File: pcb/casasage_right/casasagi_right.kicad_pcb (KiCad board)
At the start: 2 copper layers, 133.3 x 82.7 mm, 114 parts, among them J1 USB_C_Receptacle_USB2.0, J2 AudioJack4, J3 Conn_01x05, SW1 RESET, SW2 BOOT, U1 TLV73333PDBV, U2 STM32F072C8Tx, U3 AT24CS32-XHM, Y1 8MHz

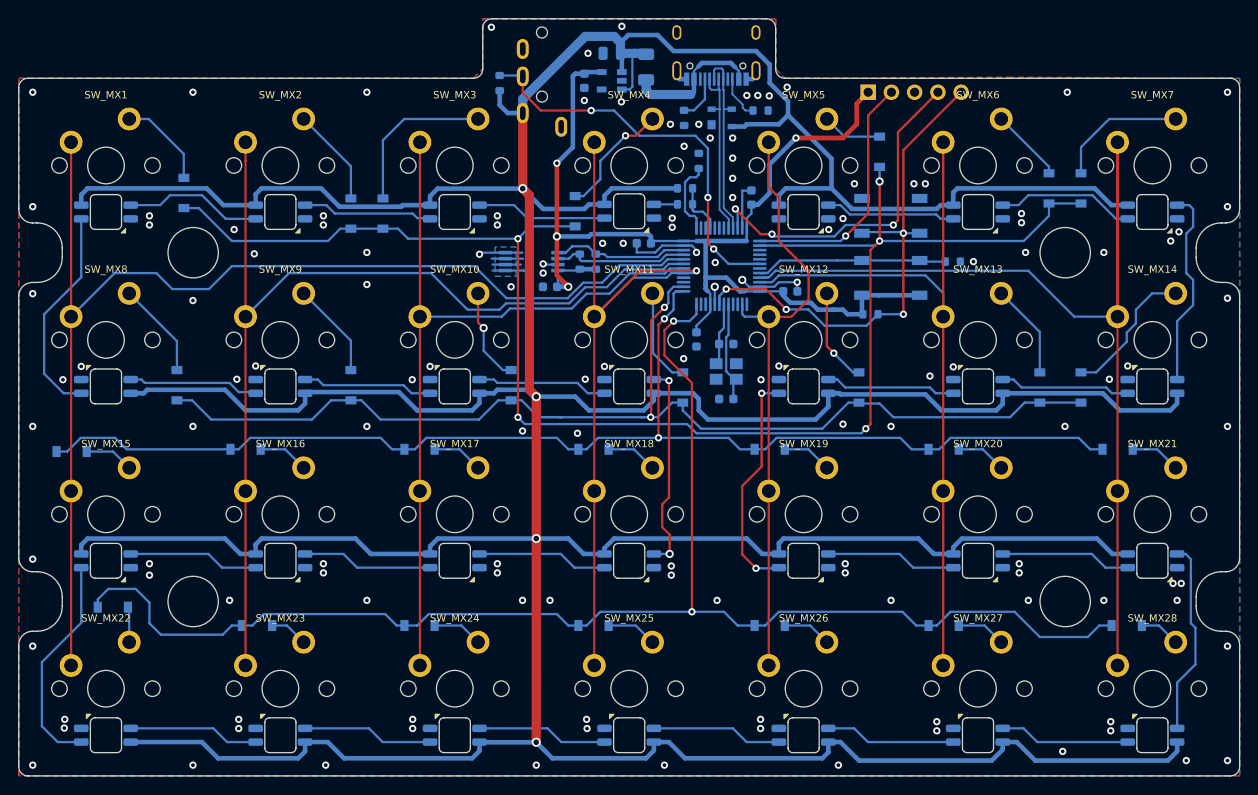
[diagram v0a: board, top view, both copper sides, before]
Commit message: update reference number for panelization
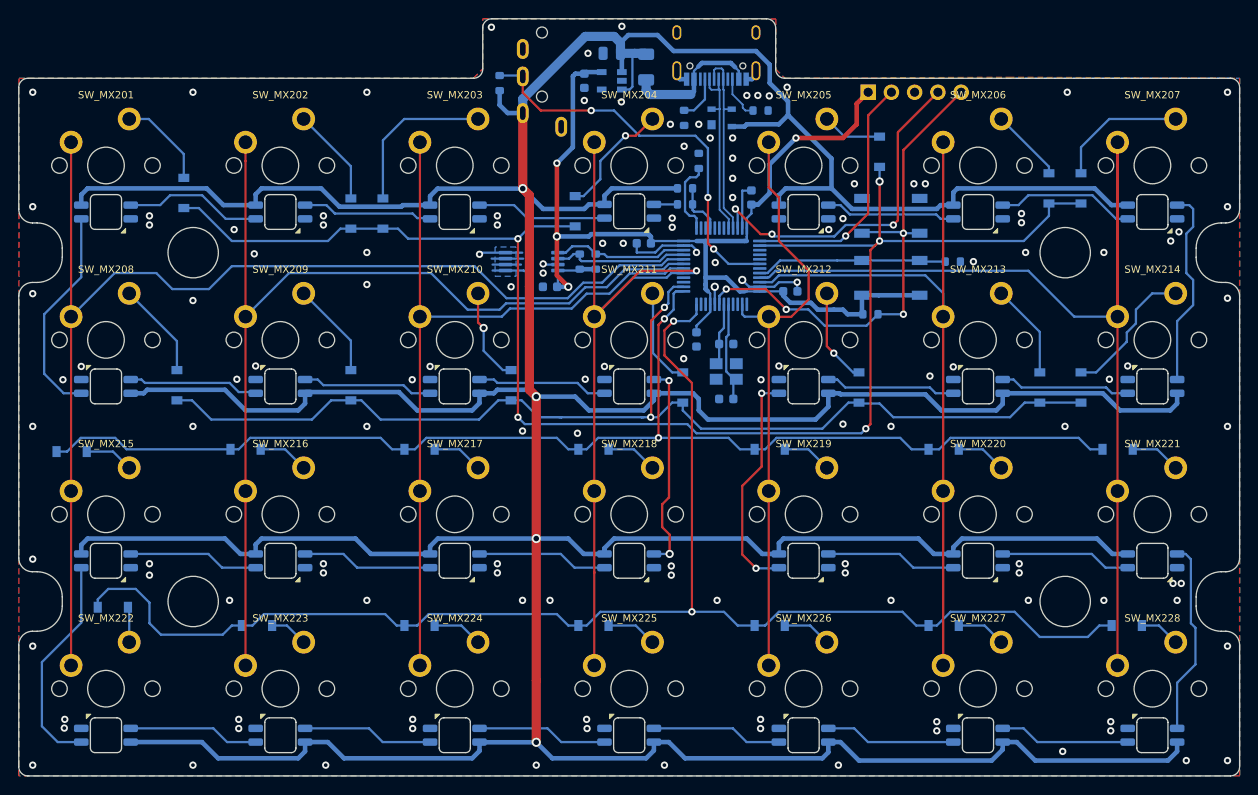
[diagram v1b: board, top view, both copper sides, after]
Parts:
- renumbered C1 to C201, C2 to C202, C9 to C203, C7 to C204, C3 to C205, C4 to C206, C5 to C207, C6 to C208, C8 to C209, D1 to D201, D2 to D202, D3 to D203, D4 to D204, D5 to D205, D6 to D206, D7 to D207, D8 to D208, D9 to D209, D10 to D210, D11 to D211, D12 to D212, D13 to D213, D14 to D214, D15 to D215, D16 to D216, D17 to D217, D18 to D218, D19 to D219, D20 to D220, D21 to D221, D22 to D222, D23 to D223, D24 to D224, D25 to D225, D26 to D226, D27 to D227, D28 to D228, D29 to D229, F1 to F201, J1 to J201, J2 to J202, J3 to J203, LED1 to LED201, LED2 to LED202, LED3 to LED203, LED4 to LED204, LED5 to LED205, LED6 to LED206, LED7 to LED207, LED8 to LED208, LED9 to LED209, LED10 to LED210, LED11 to LED211, LED12 to LED212, LED13 to LED213, LED14 to LED214, LED15 to LED215, LED16 to LED216, LED17 to LED217, LED18 to LED218, LED19 to LED219, LED20 to LED220, LED21 to LED221, LED22 to LED222, LED23 to LED223, LED24 to LED224, LED25 to LED225, LED26 to LED226, LED27 to LED227, LED28 to LED228, R1 to R201, R2 to R202, R6 to R203, R7 to R204, R3 to R205, R4 to R206, R9 to R207, R5 to R208, R10 to R209, R8 to R210, SW1 to SW201, SW2 to SW202, SW_MX1 to SW_MX201, SW_MX2 to SW_MX202, SW_MX3 to SW_MX203, SW_MX4 to SW_MX204, SW_MX5 to SW_MX205, SW_MX6 to SW_MX206, SW_MX7 to SW_MX207, SW_MX8 to SW_MX208, SW_MX9 to SW_MX209, SW_MX10 to SW_MX210, SW_MX11 to SW_MX211, SW_MX12 to SW_MX212, SW_MX13 to SW_MX213, SW_MX14 to SW_MX214, SW_MX15 to SW_MX215, SW_MX16 to SW_MX216, SW_MX17 to SW_MX217, SW_MX18 to SW_MX218, SW_MX19 to SW_MX219, SW_MX20 to SW_MX220, SW_MX21 to SW_MX221, SW_MX22 to SW_MX222, SW_MX23 to SW_MX223, SW_MX24 to SW_MX224, SW_MX25 to SW_MX225, SW_MX26 to SW_MX226, SW_MX27 to SW_MX227, SW_MX28 to SW_MX228, U1 to U201, U3 to U202, U2 to U203, Y1 to Y201

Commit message: add copyright on pcbs
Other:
- board text added: "(c) 2020, SMKiJ Casasagi Contributors"
- board text added: "Casasagi Right PCB / Rev. Alpha"
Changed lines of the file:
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@@
   (general
     (thickness 1.6)
-    (drawings 60)
+    (drawings 62)
     (tracks 1040)
     (zones 0)
@@
     (add_net "Net-(F201-Pad2)")
     (add_net "Net-(J201-PadA5)")
-    (add_net "Net-(J201-PadA8)")
     (add_net "Net-(J201-PadB5)")
-    (add_net "Net-(J201-PadB8)")
-    (add_net "Net-(J202-PadR2)")
     (add_net "Net-(LED201-Pad2)")
     (add_net "Net-(LED201-Pad4)")
@@
     (add_net "Net-(LED226-Pad2)")
     (add_net "Net-(LED227-Pad2)")
-    (add_net "Net-(LED228-Pad2)")
     (add_net "Net-(R202-Pad1)")
     (add_net "Net-(R209-Pad1)")
-    (add_net "Net-(U201-Pad4)")
-    (add_net "Net-(U203-Pad1)")
-    (add_net "Net-(U203-Pad10)")
-    (add_net "Net-(U203-Pad11)")
-    (add_net "Net-(U203-Pad15)")
-    (add_net "Net-(U203-Pad16)")
-    (add_net "Net-(U203-Pad26)")
-    (add_net "Net-(U203-Pad27)")
-    (add_net "Net-(U203-Pad29)")
-    (add_net "Net-(U203-Pad3)")
-    (add_net "Net-(U203-Pad30)")
-    (add_net "Net-(U203-Pad31)")
-    (add_net "Net-(U203-Pad39)")
-    (add_net "Net-(U203-Pad4)")
-    (add_net "Net-(U203-Pad40)")
-    (add_net "Net-(U203-Pad41)")
-    (add_net "Net-(U203-Pad43)")
   )
   (module SMKiJ_keyboard:SW_Cherry_MX_1.00u_PCB (layer F.Cu)
@@
     (descr "Through hole straight pin header, 1x05, 2.54mm pitch, single row")
     (tags "Through hole pin header THT 1x05 2.54mm single row")
-    (fp_text reference J203 (at 0 2.33 270) (layer B.SilkS)
+    (fp_text reference J203 (at 0.5 2.33 270) (layer B.SilkS)
       (effects (font (size 0.8 0.8) (thickness 0.15)) (justify mirror))
     )
@@
     )
   )
+  (gr_text "Casasagi Right PCB / Rev. Alpha" (at 171.75 42) (layer B.SilkS)
+    (effects (font (size 1 1) (thickness 0.15)) (justify left mirror))
+  )
+  (gr_text "(c) 2020, SMKiJ Casasagi Contributors" (at 77 42) (layer B.SilkS)
+    (effects (font (size 1 1) (thickness 0.15)) (justify left mirror))
+  )
   (dimension 6.5 (width 0.15) (layer Cmts.User)
     (gr_text "6.500 mm" (at 88.425 37.225 90) (layer Cmts.User)
@@
   (via (at 167.2 57.25) (size 0.8) (drill 0.4) (layers F.Cu B.Cu) (net 2))
   (via (at 42 42) (size 0.8) (drill 0.4) (layers F.Cu B.Cu) (net 2))
-  (via (at 59.5 42) (size 0.8) (drill 0.4) (layers F.Cu B.Cu) (net 2))
+  (via (at 59.5 45) (size 0.8) (drill 0.4) (layers F.Cu B.Cu) (net 2))
   (via (at 78.5 42) (size 0.8) (drill 0.4) (layers F.Cu B.Cu) (net 2))
-  (via (at 155 42) (size 0.8) (drill 0.4) (layers F.Cu B.Cu) (net 2))
+  (via (at 154.75 44.75) (size 0.8) (drill 0.4) (layers F.Cu B.Cu) (net 2))
   (via (at 172.5 42) (size 0.8) (drill 0.4) (layers F.Cu B.Cu) (net 2))
   (via (at 172.5 54.5) (size 0.8) (drill 0.4) (layers F.Cu B.Cu) (net 2))
@@
   (segment (start 111.204356 59.75) (end 110.5044 60.449956) (width 0.25) (layer B.Cu) (net 23))
   (segment (start 113.0875 59.75) (end 111.204356 59.75) (width 0.25) (layer B.Cu) (net 23))
-  (segment (start 117.75 72.5) (end 118.5 73.25) (width 0.25) (layer B.Cu) (net 84))
-  (segment (start 117.75 68.75) (end 117.75 72.5) (width 0.25) (layer B.Cu) (net 84))
-  (segment (start 118 68.5) (end 117.75 68.75) (width 0.25) (layer B.Cu) (net 84))
-  (segment (start 118 65.1625) (end 118 68.5) (width 0.25) (layer B.Cu) (net 84))
-  (segment (start 118.525 73.675) (end 118.85 73.35) (width 0.25) (layer B.Cu) (net 84))
-  (segment (start 118.525 75.5) (end 118.525 73.675) (width 0.25) (layer B.Cu) (net 84))
-  (segment (start 117.5 65.1625) (end 117.5 67.75) (width 0.25) (layer B.Cu) (net 85))
-  (segment (start 116.975 68.275) (end 116.975 69.5) (width 0.25) (layer B.Cu) (net 85))
-  (segment (start 117.5 67.75) (end 116.975 68.275) (width 0.25) (layer B.Cu) (net 85))
-  (segment (start 116.975 71.325) (end 116.65 71.65) (width 0.25) (layer B.Cu) (net 85))
-  (segment (start 116.975 69.5) (end 116.975 71.325) (width 0.25) (layer B.Cu) (net 85))
   (segment (start 58.5 48.75) (end 58.5 51.35) (width 0.25) (layer B.Cu) (net 24))
   (segment (start 54.67 44.92) (end 58.5 48.75) (width 0.25) (layer B.Cu) (net 24))
@@
   (segment (start 129.875 60.375) (end 132.575 60.375) (width 0.25) (layer B.Cu) (net 83))
   (segment (start 121.4125 61.75) (end 122.25 61.75) (width 0.25) (layer B.Cu) (net 83))
+  (segment (start 117.75 72.5) (end 118.5 73.25) (width 0.25) (layer B.Cu) (net 84))
+  (segment (start 117.75 68.75) (end 117.75 72.5) (width 0.25) (layer B.Cu) (net 84))
+  (segment (start 118 68.5) (end 117.75 68.75) (width 0.25) (layer B.Cu) (net 84))
+  (segment (start 118 65.1625) (end 118 68.5) (width 0.25) (layer B.Cu) (net 84))
+  (segment (start 118.525 73.675) (end 118.85 73.35) (width 0.25) (layer B.Cu) (net 84))
+  (segment (start 118.525 75.5) (end 118.525 73.675) (width 0.25) (layer B.Cu) (net 84))
+  (segment (start 117.5 65.1625) (end 117.5 67.75) (width 0.25) (layer B.Cu) (net 85))
+  (segment (start 116.975 68.275) (end 116.975 69.5) (width 0.25) (layer B.Cu) (net 85))
+  (segment (start 117.5 67.75) (end 116.975 68.275) (width 0.25) (layer B.Cu) (net 85))
+  (segment (start 116.975 71.325) (end 116.65 71.65) (width 0.25) (layer B.Cu) (net 85))
+  (segment (start 116.975 69.5) (end 116.975 71.325) (width 0.25) (layer B.Cu) (net 85))
   (segment (start 114.5 56.8375) (end 114.5 55.75) (width 0.25) (layer B.Cu) (net 86))
   (segment (start 114.5 55.75) (end 114.25 55.5) (width 0.25) (layer B.Cu) (net 86))

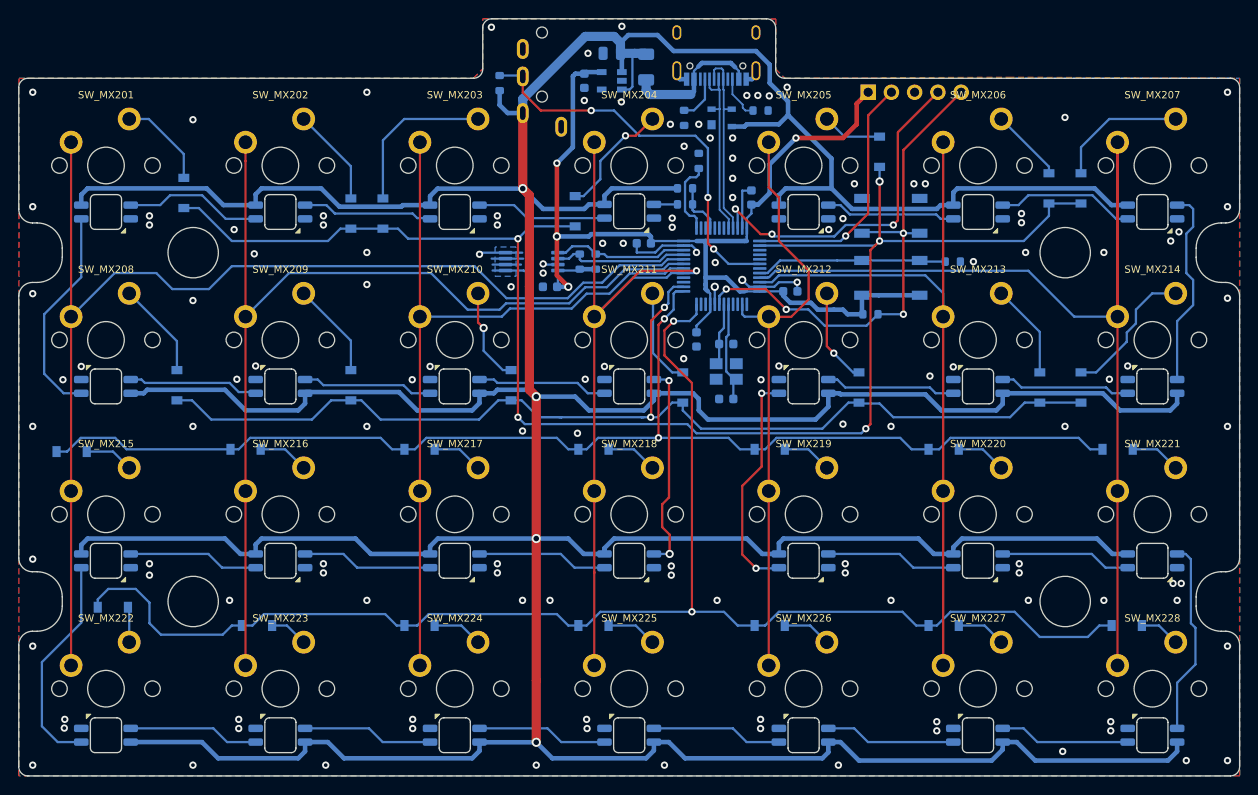
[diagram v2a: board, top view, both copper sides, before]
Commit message: add teardrops to right pcb
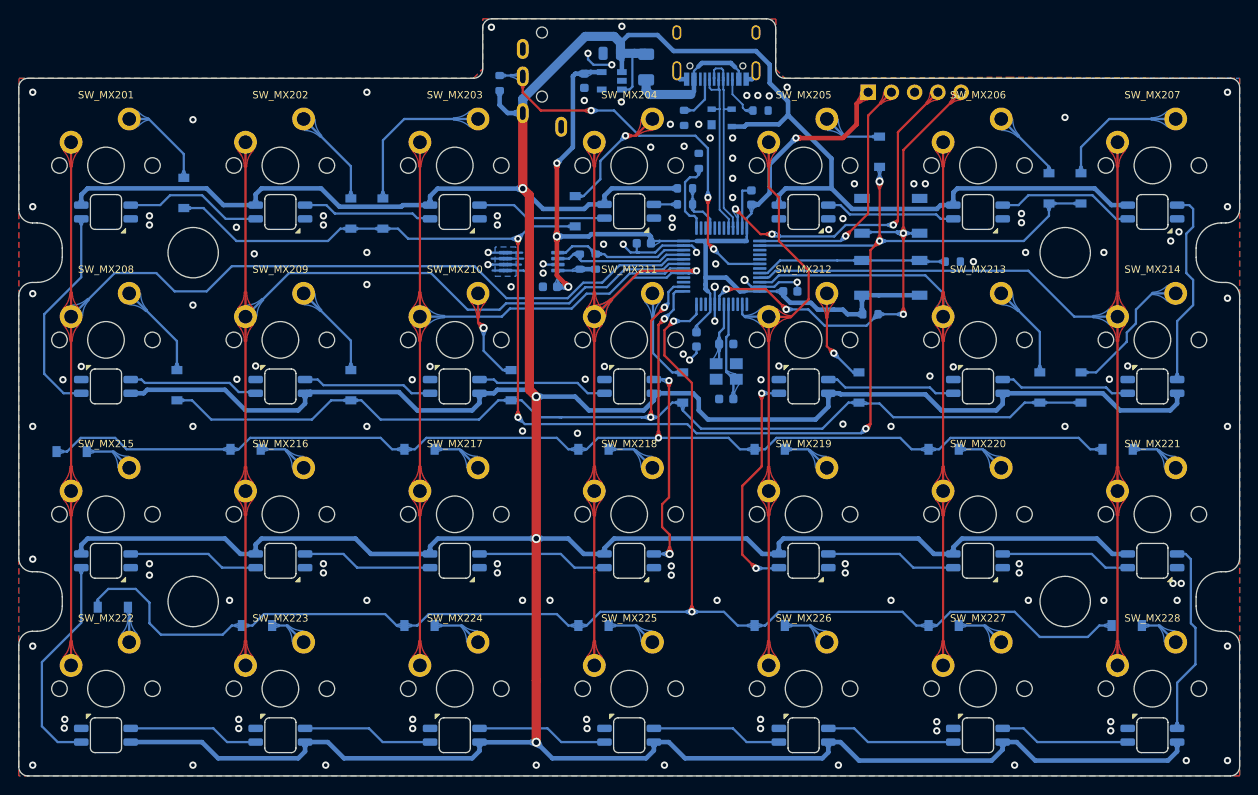
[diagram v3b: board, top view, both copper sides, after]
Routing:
- net /COL6: track 117.7 -> 98.6 mm
- net GND: track 42.8 -> 51.4 mm, vias 135 -> 140

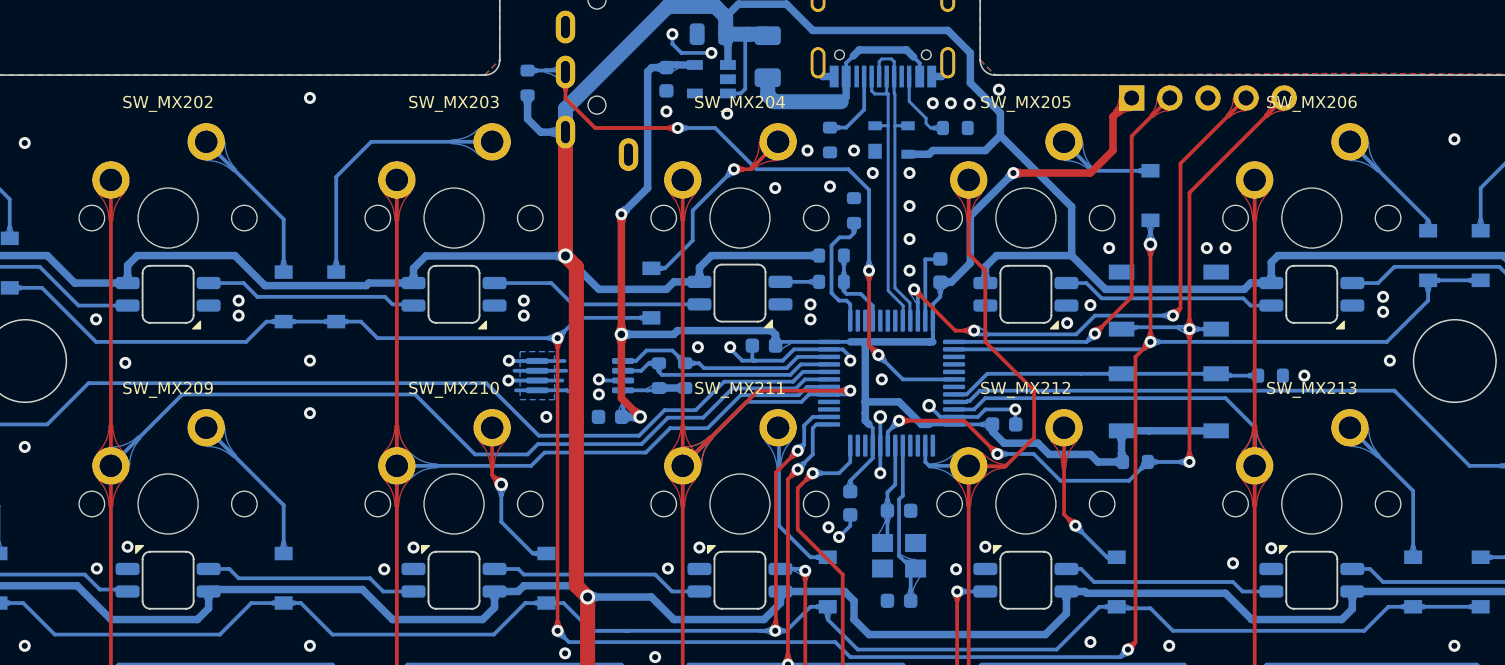
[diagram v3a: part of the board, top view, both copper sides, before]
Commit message: add teardrop and adjust trace
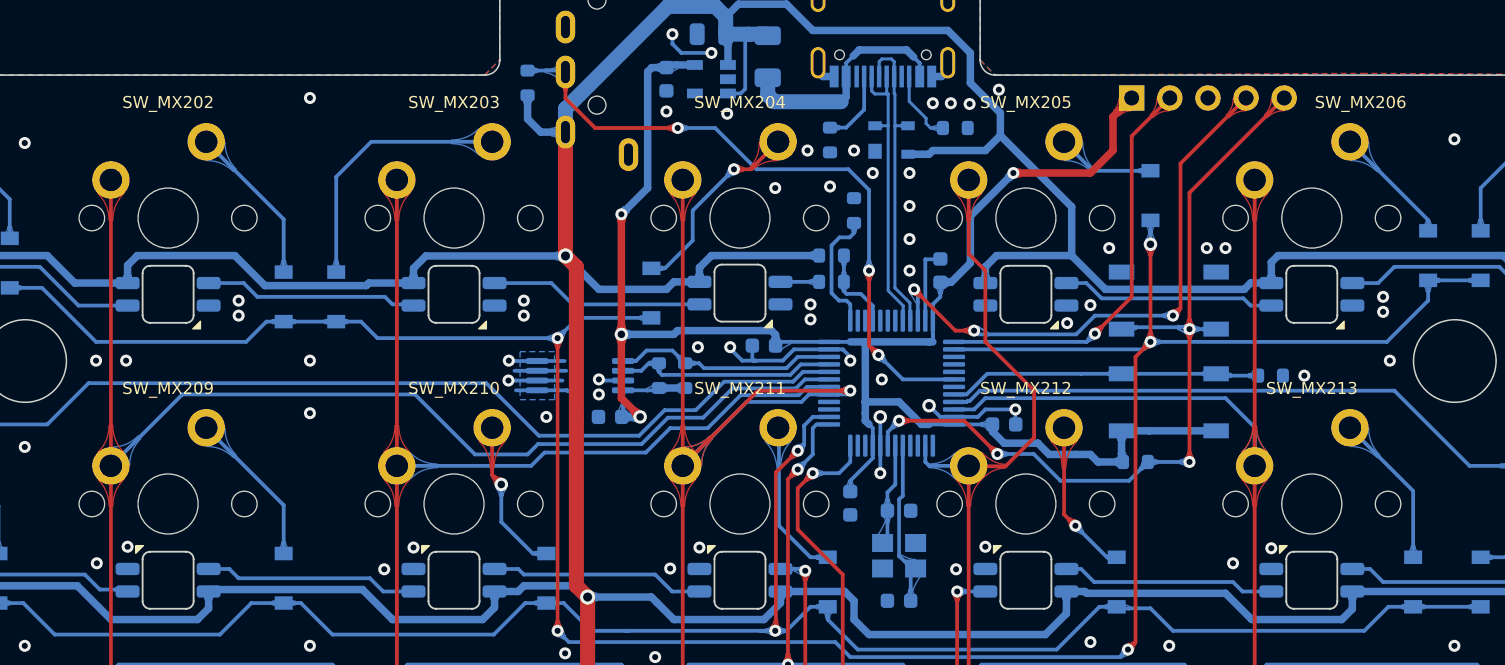
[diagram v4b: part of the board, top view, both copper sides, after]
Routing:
- net GND: track 51.4 -> 49.6 mm, vias 140 -> 138
